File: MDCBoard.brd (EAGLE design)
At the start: 43.9 x 32.6 mm, 200 parts, among them J1 JUMPER-SOLDER, J10 MICROSD-SOCKET, J11 USB-C-RECEPTACLE-KOREANHRO, J2 JUMPER-SOLDER, J3 JUMPER-SOLDER, J4 JUMPER-SOLDER, J5 JST-SM02B-SRSS-TB, J6 JUMPER-SOLDER, J7 JUMPER-SOLDER, J8 JUMPER-SOLDER, Q1 PMOS-NEXPERIA-SOT1220, Q2 PMOS-NEXPERIA-SOT1220, Q3 PMOS-NEXPERIA-SOT1220, Q4 DIODESINC-DMG2305UX, Q5 DIODESINC-DMG2305UX, Q6 DIODESINC-DMG2305UX, Q7 DIODESINC-DMG2305UX, Q8 DIODESINC-DMG2305UX, U1 TI-TPS2116, U10 TI-TPS22919DCK, U11 TI-TPS22919DCK, U12 TI-TPS22919DCK, U13 TI-TPS22919DCK, U14 TI-MSP430FR2422IRHL, U16 TI-TXB0102, U17 PANASONIC-EKMB110711X, U18 LATTICE-ICE40HX4K-BG121, U19 WINBOND-W25Q40EW, U2 DIODESINC-AP7350, U20 NEXPERIA-74LVC1G98-OR-INV-INP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, U21 NEXPERIA-74LVC1G98-BUFFER, U22 ON-AR0330CS1C12SPKA0, U23 ALLIANCE-AS4C8M16MSA-6BIN, U24 STM-STM32F730, U25 DIODESINC-DT1446-04V-7, U26 NEXPERIA-74LVC1G98-INVERTER, U3 NEXPERIA-74LVC1G98-NOR, U4 MICROCHIP-MCP7383X, U5 NEXPERIA-74LVC1G98-INVERTER, U6 EATON-STN101, U7 TI-TPS62A01, U8 TI-TPS62A01, U9 TI-TPS62A01, X1 EPSON-FC-135, X2 SITIME-SIT8021, X3 SITIME-SIT8021

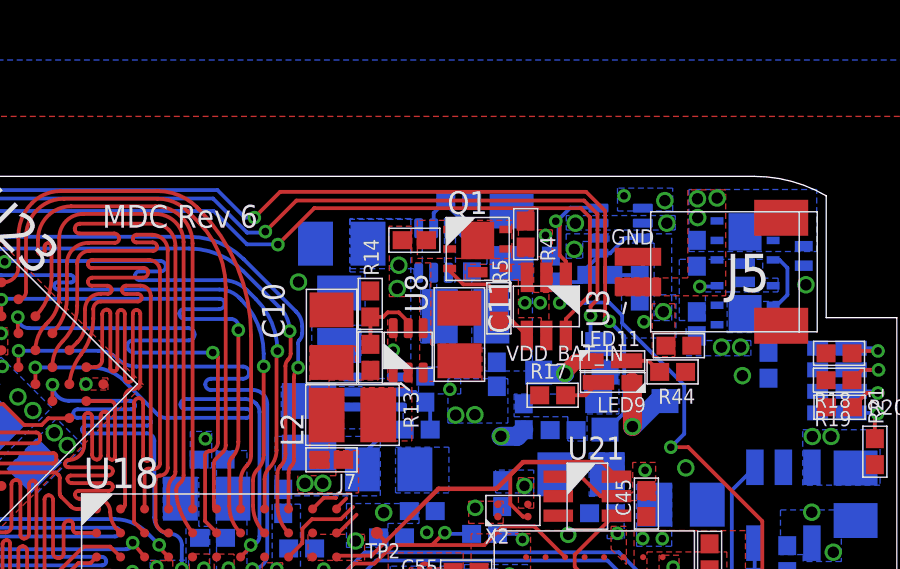
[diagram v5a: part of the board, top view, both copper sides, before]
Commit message: 14 airwires
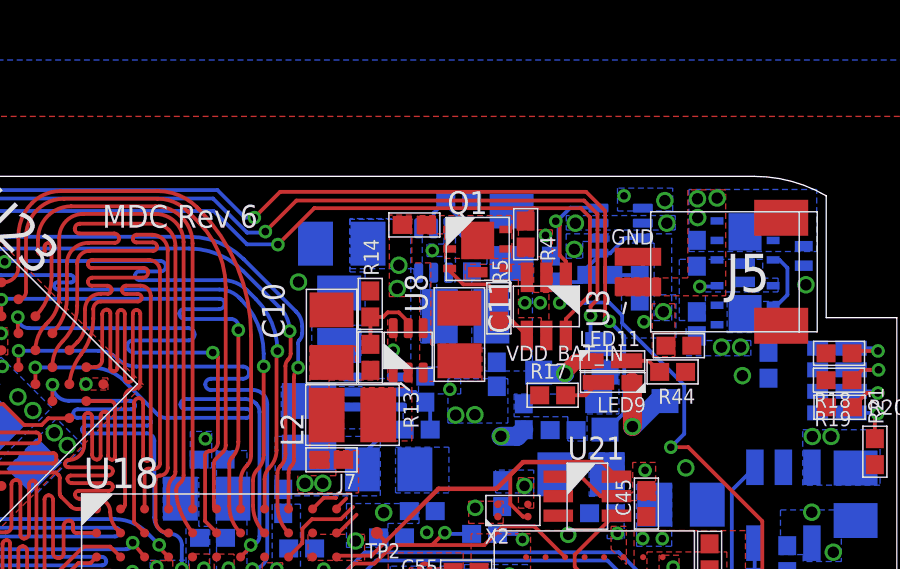
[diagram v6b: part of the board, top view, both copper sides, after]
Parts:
- moved J3 0.51 mm to (27.8, 31.0)
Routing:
- net GND: vias 72 -> 73
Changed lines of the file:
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@@
 <grid distance="10" unitdist="mil" unit="mil" style="lines" multiple="1" display="no" altdistance="0.00254" altunitdist="mm" altunit="mil"/>
 <layers>
-<layer number="1" name="Top" color="4" fill="1" visible="yes" active="yes"/>
+<layer number="1" name="Top" color="4" fill="1" visible="no" active="yes"/>
 <layer number="2" name="Ground" color="16" fill="1" visible="no" active="yes"/>
 <layer number="3" name="Route3" color="17" fill="1" visible="no" active="no"/>
@@
 <layer number="14" name="Route14" color="22" fill="1" visible="no" active="no"/>
 <layer number="15" name="Power" color="42" fill="1" visible="no" active="yes"/>
-<layer number="16" name="Bottom" color="1" fill="1" visible="no" active="yes"/>
+<layer number="16" name="Bottom" color="1" fill="1" visible="yes" active="yes"/>
 <layer number="17" name="Pads" color="2" fill="1" visible="yes" active="yes"/>
 <layer number="18" name="Vias" color="2" fill="1" visible="yes" active="yes"/>
 <layer number="19" name="Unrouted" color="6" fill="1" visible="no" active="yes"/>
 <layer number="20" name="Dimension" color="24" fill="1" visible="yes" active="yes"/>
-<layer number="21" name="tPlace" color="7" fill="1" visible="yes" active="yes"/>
-<layer number="22" name="bPlace" color="7" fill="1" visible="no" active="yes"/>
-<layer number="23" name="tOrigins" color="15" fill="1" visible="yes" active="yes"/>
-<layer number="24" name="bOrigins" color="15" fill="1" visible="no" active="yes"/>
-<layer number="25" name="tNames" color="7" fill="1" visible="yes" active="yes"/>
-<layer number="26" name="bNames" color="7" fill="1" visible="no" active="yes"/>
-<layer number="27" name="tValues" color="7" fill="1" visible="yes" active="yes"/>
-<layer number="28" name="bValues" color="7" fill="1" visible="no" active="yes"/>
-<layer number="29" name="tStop" color="7" fill="3" visible="yes" active="yes"/>
-<layer number="30" name="bStop" color="7" fill="6" visible="no" active="yes"/>
-<layer number="31" name="tCream" color="7" fill="4" visible="yes" active="yes"/>
-<layer number="32" name="bCream" color="7" fill="5" visible="no" active="yes"/>
-<layer number="33" name="tFinish" color="6" fill="3" visible="yes" active="yes"/>
-<layer number="34" name="bFinish" color="6" fill="6" visible="no" active="yes"/>
-<layer number="35" name="tGlue" color="7" fill="4" visible="yes" active="yes"/>
-<layer number="36" name="bGlue" color="7" fill="5" visible="no" active="yes"/>
-<layer number="37" name="tTest" color="7" fill="1" visible="yes" active="yes"/>
-<layer number="38" name="bTest" color="7" fill="1" visible="no" active="yes"/>
-<layer number="39" name="tKeepout" color="4" fill="11" visible="yes" active="yes"/>
-<layer number="40" name="bKeepout" color="1" fill="11" visible="no" active="yes"/>
-<layer number="41" name="tRestrict" color="4" fill="10" visible="yes" active="yes"/>
-<layer number="42" name="bRestrict" color="1" fill="10" visible="no" active="yes"/>
+<layer number="21" name="tPlace" color="7" fill="1" visible="no" active="yes"/>
+<layer number="22" name="bPlace" color="7" fill="1" visible="yes" active="yes"/>
+<layer number="23" name="tOrigins" color="15" fill="1" visible="no" active="yes"/>
+<layer number="24" name="bOrigins" color="15" fill="1" visible="yes" active="yes"/>
+<layer number="25" name="tNames" color="7" fill="1" visible="no" active="yes"/>
+<layer number="26" name="bNames" color="7" fill="1" visible="yes" active="yes"/>
+<layer number="27" name="tValues" color="7" fill="1" visible="no" active="yes"/>
+<layer number="28" name="bValues" color="7" fill="1" visible="yes" active="yes"/>
+<layer number="29" name="tStop" color="7" fill="3" visible="no" active="yes"/>
+<layer number="30" name="bStop" color="7" fill="6" visible="yes" active="yes"/>
+<layer number="31" name="tCream" color="7" fill="4" visible="no" active="yes"/>
+<layer number="32" name="bCream" color="7" fill="5" visible="yes" active="yes"/>
+<layer number="33" name="tFinish" color="6" fill="3" visible="no" active="yes"/>
+<layer number="34" name="bFinish" color="6" fill="6" visible="yes" active="yes"/>
+<layer number="35" name="tGlue" color="7" fill="4" visible="no" active="yes"/>
+<layer number="36" name="bGlue" color="7" fill="5" visible="yes" active="yes"/>
+<layer number="37" name="tTest" color="7" fill="1" visible="no" active="yes"/>
+<layer number="38" name="bTest" color="7" fill="1" visible="yes" active="yes"/>
+<layer number="39" name="tKeepout" color="4" fill="11" visible="no" active="yes"/>
+<layer number="40" name="bKeepout" color="1" fill="11" visible="yes" active="yes"/>
+<layer number="41" name="tRestrict" color="4" fill="10" visible="no" active="yes"/>
+<layer number="42" name="bRestrict" color="1" fill="10" visible="yes" active="yes"/>
 <layer number="43" name="vRestrict" color="2" fill="10" visible="no" active="yes"/>
 <layer number="44" name="Drills" color="7" fill="1" visible="no" active="yes"/>
@@
 <attribute name="PN" value="PMPB10UPX" x="29.882984375" y="30.230321875" size="1.778" layer="27" display="off"/>
 </element>
-<element name="J3" library="EagleLibrary" package="JUMPER-SOLDER" value="JUMPER-SOLDER" x="27.772425" y="30.522221875" smashed="yes" rot="R180" grouprefs="_VDD_B_CONTROL"/>
+<element name="J3" library="EagleLibrary" package="JUMPER-SOLDER" value="JUMPER-SOLDER" x="27.772425" y="31.030221875" smashed="yes" rot="R180" grouprefs="_VDD_B_CONTROL"/>
 <element name="U3" library="EagleLibrary" package="NEXPERIA-SOT363" value="NEXPERIA-74LVC1G98-NOR" x="32.171109375" y="28.315165625" smashed="yes" rot="R270" grouprefs="_VDD_B_CONTROL">
 <attribute name="MFG" value="Nexperia" x="32.171109375" y="28.315165625" size="1.778" layer="27" rot="R270" display="off"/>
@@
 <vertex x="28.322021875" y="29.766259375"/>
 <vertex x="27.686" y="29.766259375"/>
-<vertex x="27.686" y="30.988"/>
-<vertex x="26.924" y="30.988"/>
-<vertex x="26.93771875" y="30.97428125"/>
+<vertex x="27.686" y="31.358840625"/>
+<vertex x="26.93771875" y="31.358840625"/>
 <vertex x="26.93771875" y="28.64358125"/>
 <vertex x="27.948640625" y="28.64358125"/>
@@
 <vertex x="25.99538125" y="27.559"/>
 </polygon>
-<polygon width="0.127" layer="16" thermals="no">
+<polygon width="0.127" layer="16" thermals="no" rank="2">
 <vertex x="25.6347" y="31.216603125"/>
 <vertex x="25.6347" y="29.57321875"/>
@@
 <vertex x="24.2504" y="5.222240625"/>
 </polygon>
-<polygon width="0.127" layer="16" thermals="no" rank="2">
-<vertex x="28.7741375" y="31.242"/>
-<vertex x="28.7741375" y="29.12871875"/>
-<vertex x="29.142440625" y="29.12871875"/>
+<polygon width="0.127" layer="16" thermals="no">
 <vertex x="29.142440625" y="31.242"/>
+<vertex x="28.76041875" y="31.242"/>
+<vertex x="28.76041875" y="30.393640625"/>
+<vertex x="28.194" y="30.393640625"/>
+<vertex x="28.194" y="29.979621875"/>
+<vertex x="28.782053125" y="29.979621875"/>
+<vertex x="28.782053125" y="29.12871875"/>
+<vertex x="29.142440625" y="29.12871875"/>
 </polygon>
 <via x="24.75078125" y="19.558" extent="1-16" drill="0.254"/>
@@
 <via x="37.592" y="16.764" extent="1-16" drill="0.381"/>
 <via x="38.707059375" y="26.007059375" extent="1-16" drill="0.381"/>
+<via x="28.374340625" y="30.1777375" extent="1-16" drill="0.254"/>
 <wire x1="27.192578125" y1="24.960959375" x2="27.0676375" y2="26.110340625" width="0" layer="19" extent="1-16"/>
-<wire x1="28.916" y1="30.917740625" x2="29.6841625" y2="31.831278125" width="0" layer="19" extent="16-16"/>
 <wire x1="29.2735" y1="28.2537375" x2="28.916" y2="29.437740625" width="0" layer="19" extent="1-16"/>
 <wire x1="21.93470625" y1="5.83590625" x2="21.030403125" y2="4.67901875" width="0" layer="19" extent="1-16"/>
@@
 <contactref element="J3" pad="1"/>
 <polygon width="0.127" layer="1" thermals="no" rank="2">
-<vertex x="27.873959375" y="31.18358125"/>
-<vertex x="27.873959375" y="29.91358125"/>
+<vertex x="31.023559375" y="31.3436"/>
+<vertex x="27.8866625" y="31.3436"/>
+<vertex x="27.8866625" y="30.734"/>
+<vertex x="28.7782" y="30.734"/>
+<vertex x="28.7782" y="29.91358125"/>
 <vertex x="31.023559375" y="29.91358125"/>
-<vertex x="31.023559375" y="31.18358125"/>
 </polygon>
 </signal>

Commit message: 13 airwires
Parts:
- moved C22 0.72 mm to (18.8, 3.19), turned to 90 degrees
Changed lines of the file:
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@@
 <attribute name="PN" value="MSP430FR2422IRHL" x="11.493478125" y="3.312359375" size="1.778" layer="27" rot="R180" display="off"/>
 </element>
-<element name="C22" library="EagleLibrary" package="0402" value="22p" x="18.96683125" y="2.48265625" smashed="yes" rot="MR180">
-<attribute name="MFG" value="Murata" x="18.96683125" y="2.48265625" size="1.778" layer="28" rot="MR180" display="off"/>
-<attribute name="NAME" x="20.983971875" y="2.391475" size="0.508" layer="26" font="vector" rot="MR0"/>
-<attribute name="PN" value="GRM1555C1H220JA01D" x="18.96683125" y="2.48265625" size="1.778" layer="28" rot="MR180" display="off"/>
+<element name="C22" library="EagleLibrary" package="0402" value="22p" x="18.8195125" y="3.191315625" smashed="yes" rot="MR90">
+<attribute name="MFG" value="Murata" x="18.8195125" y="3.191315625" size="1.778" layer="28" rot="MR90" display="off"/>
+<attribute name="NAME" x="18.91069375" y="5.20845625" size="0.508" layer="26" font="vector" rot="MR270"/>
+<attribute name="PN" value="GRM1555C1H220JA01D" x="18.8195125" y="3.191315625" size="1.778" layer="28" rot="MR90" display="off"/>
 </element>
 <element name="U10" library="EagleLibrary" package="TI-TPS22919DCK" value="TI-TPS22919DCK" x="6.27481875" y="4.97388125" smashed="yes" rot="R180">
@@
 <wire x1="29.2735" y1="28.2537375" x2="28.916" y2="29.437740625" width="0" layer="19" extent="1-16"/>
 <wire x1="21.93470625" y1="5.83590625" x2="21.030403125" y2="4.67901875" width="0" layer="19" extent="1-16"/>
-<wire x1="19.39933125" y1="2.48265625" x2="18.034" y2="3.81" width="0" layer="19" extent="16-16"/>
-<wire x1="19.398978125" y1="1.0617125" x2="19.39933125" y2="2.48265625" width="0" layer="19" extent="1-16"/>
 <wire x1="30.695915625" y1="6.69100625" x2="29.8034625" y2="4.99618125" width="0" layer="19" extent="1-1"/>
 <wire x1="28.346978125" y1="9.3113625" x2="29.8810375" y2="8.646903125" width="0" layer="19" extent="1-1"/>
+<wire x1="19.398978125" y1="1.0617125" x2="18.8195125" y2="3.623815625" width="0" layer="19" extent="1-16"/>
 </signal>
 <signal name="ICE_IMG_CLK16MHZ">
@@
 <wire x1="14.3030375" y1="1.2351625" x2="17.381546875" y2="1.2351625" width="0.127" layer="1"/>
 <contactref element="U24" pad="B8"/>
-<wire x1="18.53433125" y1="2.48265625" x2="18.074196875" y2="2.48265625" width="0.127" layer="16"/>
-<wire x1="18.074196875" y1="2.48265625" x2="17.836896875" y2="2.24535625" width="0.127" layer="16"/>
-<wire x1="18.961503125" y1="3.0342875" x2="18.53433125" y2="2.607115625" width="0.127" layer="16"/>
-<wire x1="18.53433125" y1="2.48265625" x2="18.53433125" y2="2.607115625" width="0.127" layer="16"/>
 <wire x1="22.68990625" y1="1.9586875" x2="22.860075" y2="1.78851875" width="0.127" layer="16"/>
 <wire x1="23.33990625" y1="1.3086875" x2="23.510075" y2="1.13851875" width="0.127" layer="16"/>
@@
 <wire x1="22.4359625" y1="3.0342875" x2="22.68990625" y2="2.78034375" width="0.127" layer="16"/>
 <wire x1="22.68990625" y1="2.78034375" x2="22.68990625" y2="1.9586875" width="0.127" layer="16"/>
-<wire x1="18.961503125" y1="3.0342875" x2="22.4359625" y2="3.0342875" width="0.127" layer="16"/>
+<wire x1="19.977503125" y1="3.0342875" x2="22.4359625" y2="3.0342875" width="0.127" layer="16"/>
+<wire x1="19.977503125" y1="3.0342875" x2="19.70203125" y2="2.758815625" width="0.127" layer="16"/>
+<wire x1="19.70203125" y1="2.758815625" x2="18.8195125" y2="2.758815625" width="0.127" layer="16"/>
+<wire x1="18.35035625" y1="2.758815625" x2="18.8195125" y2="2.758815625" width="0.127" layer="16"/>
+<wire x1="17.836896875" y1="2.24535625" x2="18.35035625" y2="2.758815625" width="0.127" layer="16"/>
 </signal>
 <signal name="ICE_MSP_SPI_DATA_X">
